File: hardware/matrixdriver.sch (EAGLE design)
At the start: 46 parts, among them IC1 75176AD, IC2 4017D, IC4 7805T, J1 DCJ0202, Q1 CSM-7X-DU, Q2 MMBT4403LT1SMD, Q3 MMBT4403LT1SMD, Q4 MMBT4403LT1SMD, Q5 MMBT4403LT1SMD, Q6 MMBT4403LT1SMD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

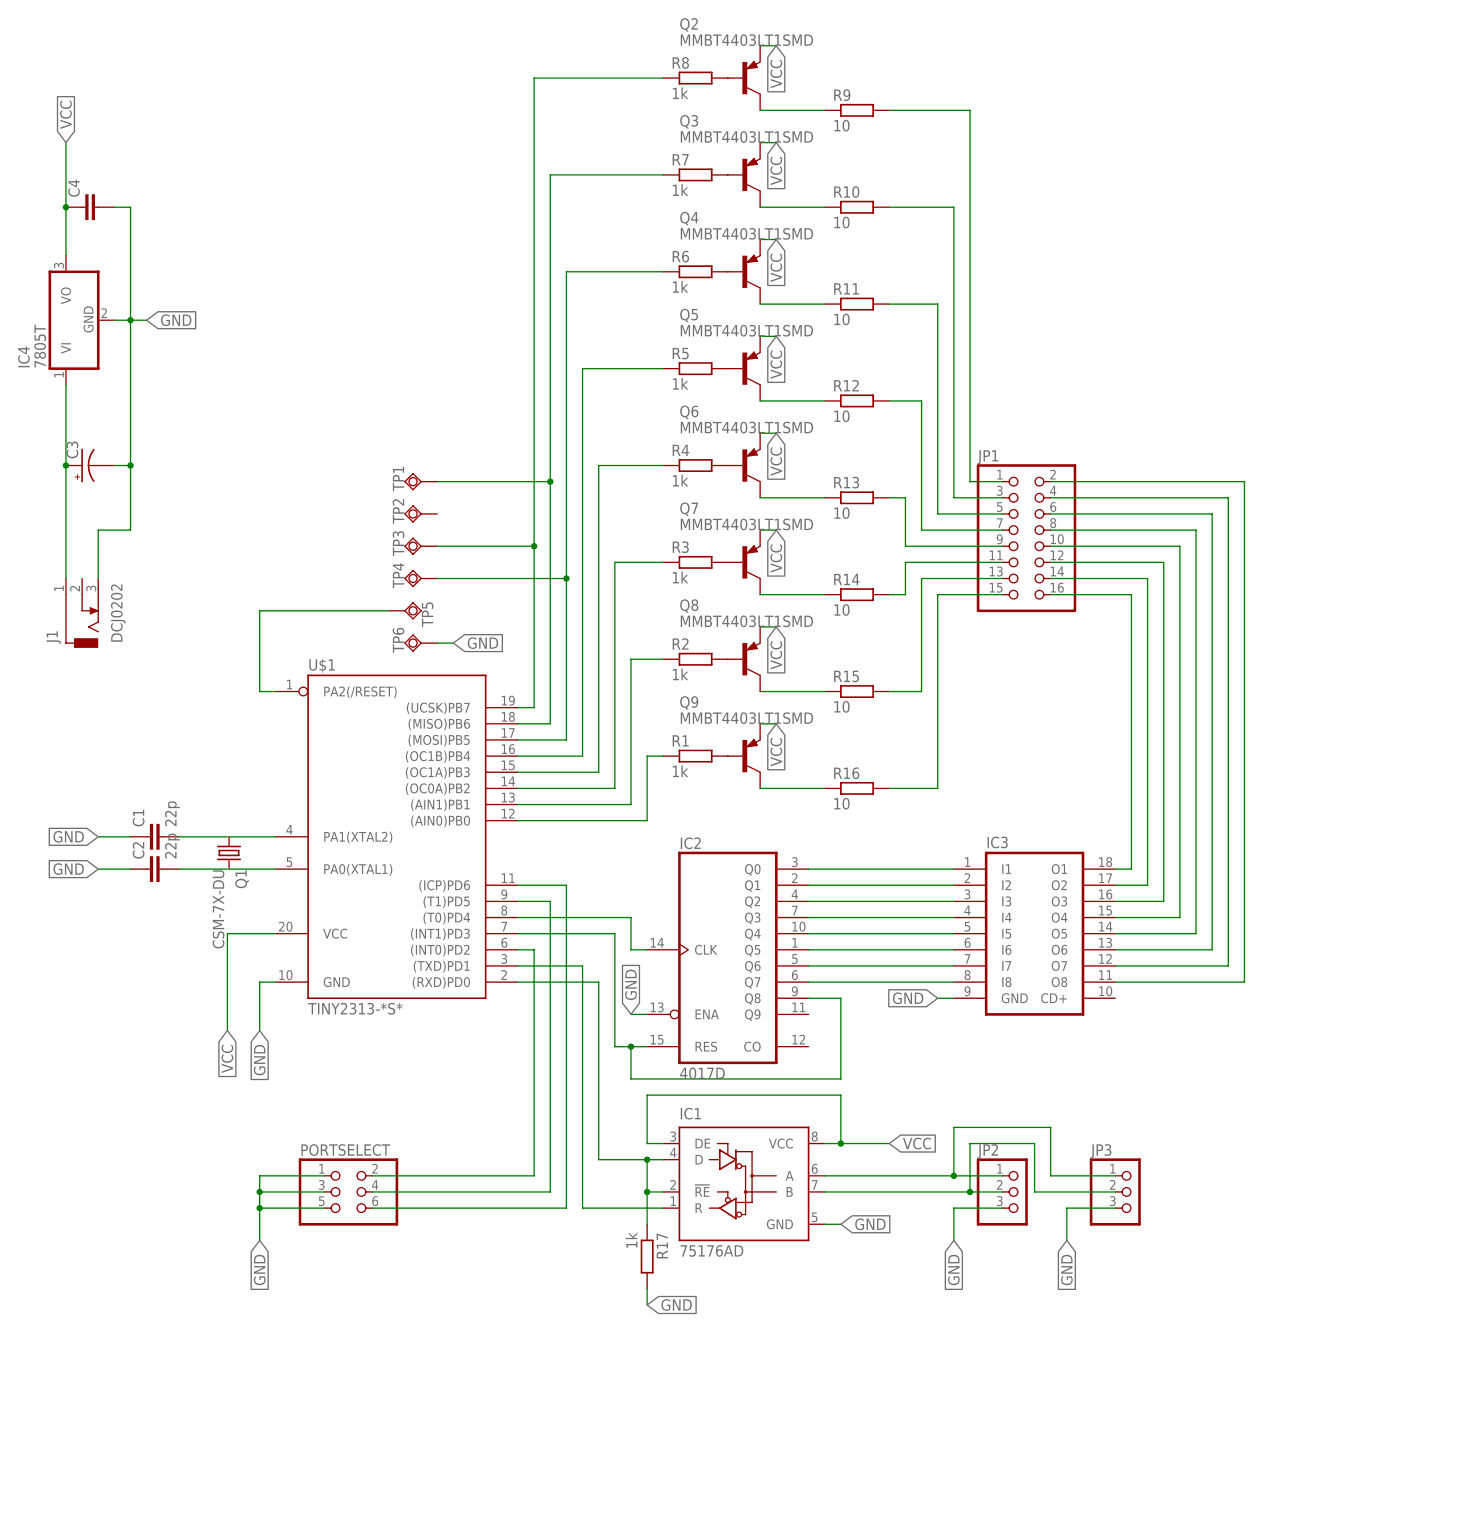
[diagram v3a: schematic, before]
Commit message: Fix Schematic ERC rrors
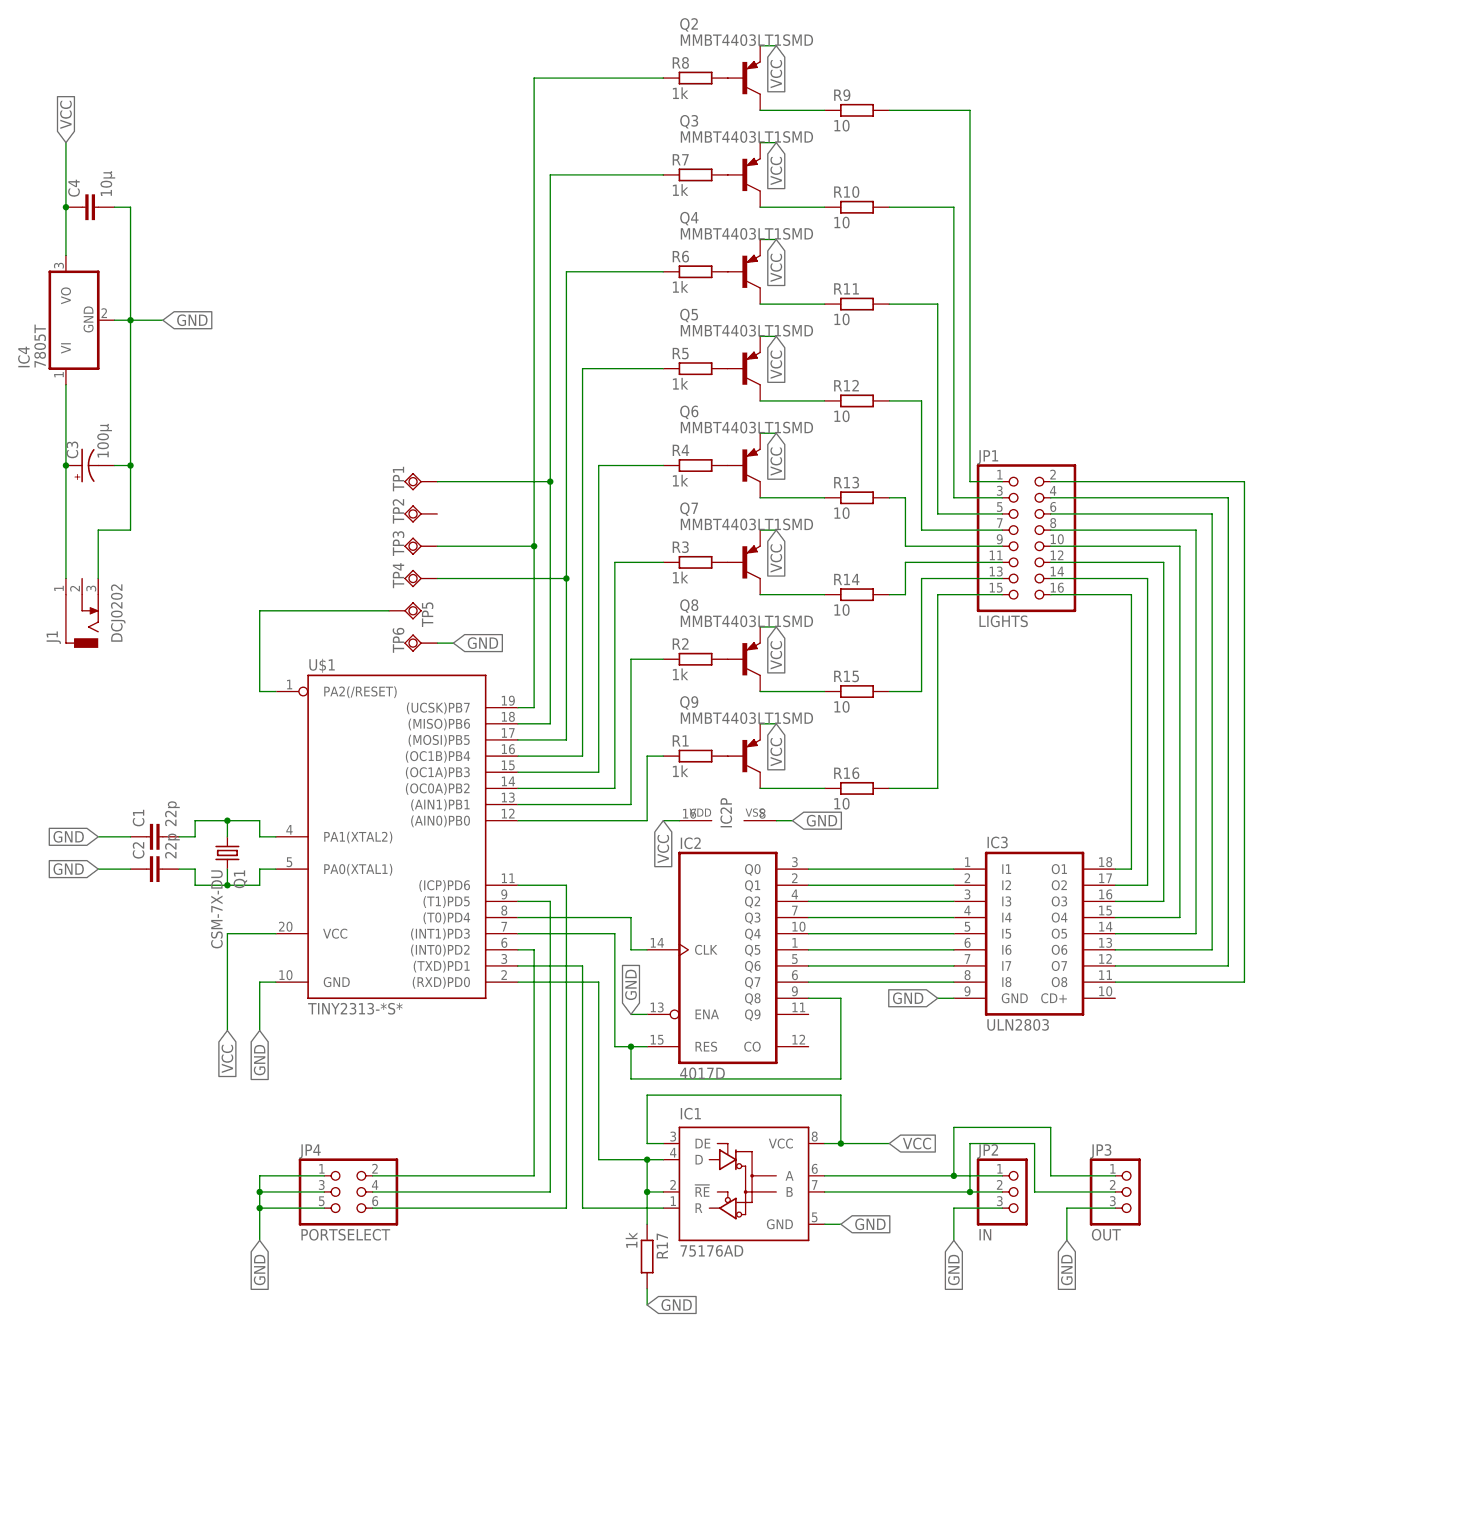
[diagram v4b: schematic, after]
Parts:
- C3: value (none) -> 100µ
- C4: value (none) -> 10µ
- IC3: value (none) -> ULN2803
- JP1: value (none) -> LIGHTS
- JP2: value (none) -> IN
- JP3: value (none) -> OUT
- JP4: value (none) -> PORTSELECT
- renumbered PORTSELECT to JP4
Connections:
- removed net N$13: C1.2
- removed net N$14: C2.2
- net GND: now also IC2P.VSS
- net N$11: now also C1.2
- net N$12: now also C2.2
- net VCC: now also IC2P.VDD
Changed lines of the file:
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@@
 <part name="C2" library="resistor" deviceset="C-EU" device="C1206" value="22p"/>
 <part name="IC2" library="40xx" deviceset="4017" device="D"/>
-<part name="IC3" library="uln-udn" deviceset="ULN2803A" device="SMD"/>
-<part name="JP1" library="pinhead-fixdrills" deviceset="PINHD-2X8" device="_2.54-90°"/>
+<part name="IC3" library="uln-udn" deviceset="ULN2803A" device="SMD" value="ULN2803"/>
+<part name="JP1" library="pinhead-fixdrills" deviceset="PINHD-2X8" device="_2.54-90°" value="LIGHTS"/>
 <part name="Q2" library="transistor-pnp" deviceset="MMBT4403*" device="SMD" technology="LT1"/>
 <part name="Q3" library="transistor-pnp" deviceset="MMBT4403*" device="SMD" technology="LT1"/>
@@
 <part name="Q8" library="transistor-pnp" deviceset="MMBT4403*" device="SMD" technology="LT1"/>
 <part name="Q9" library="transistor-pnp" deviceset="MMBT4403*" device="SMD" technology="LT1"/>
-<part name="JP2" library="pinhead" deviceset="PINHD-1X3" device=""/>
-<part name="JP3" library="pinhead" deviceset="PINHD-1X3" device=""/>
+<part name="JP2" library="pinhead" deviceset="PINHD-1X3" device="" value="IN"/>
+<part name="JP3" library="pinhead" deviceset="PINHD-1X3" device="" value="OUT"/>
 <part name="TP1" library="testpad" deviceset="TPSQ" device="TP20SQ"/>
 <part name="TP2" library="testpad" deviceset="TPSQ" device="TP20SQ"/>
@@
 <part name="TP5" library="testpad" deviceset="TPSQ" device="TP20SQ"/>
 <part name="TP6" library="testpad" deviceset="TPSQ" device="TP20SQ"/>
-<part name="PORTSELECT" library="pinhead" deviceset="PINHD-2X3" device=""/>
+<part name="JP4" library="pinhead" deviceset="PINHD-2X3" device="" value="PORTSELECT"/>
 <part name="IC4" library="linear" deviceset="78*" device="T" technology="05"/>
-<part name="C3" library="rcl" deviceset="CPOL-US" device="E5-8.5"/>
-<part name="C4" library="rcl" deviceset="C-EU" device="C1206"/>
+<part name="C3" library="rcl" deviceset="CPOL-US" device="E5-8.5" value="100µ"/>
+<part name="C4" library="rcl" deviceset="C-EU" device="C1206" value="10µ"/>
 <part name="J1" library="con-jack" deviceset="DCJ0202" device=""/>
 </parts>
@@
 <instance part="R15" gate="G$1" x="129.54" y="93.98"/>
 <instance part="R16" gate="G$1" x="129.54" y="78.74"/>
-<instance part="Q1" gate="P" x="30.734" y="68.58" rot="R270"/>
+<instance part="Q1" gate="P" x="30.48" y="68.58" rot="R270"/>
 <instance part="IC1" gate="G$1" x="111.76" y="17.78"/>
 <instance part="R17" gate="G$1" x="96.52" y="5.08" rot="R270"/>
@@
 <instance part="TP5" gate="G$1" x="58.42" y="106.68" rot="R90"/>
 <instance part="TP6" gate="G$1" x="60.96" y="101.6" rot="R270"/>
-<instance part="PORTSELECT" gate="A" x="48.26" y="15.24"/>
+<instance part="JP4" gate="A" x="48.26" y="15.24"/>
 <instance part="IC4" gate="A1" x="5.08" y="152.4" rot="R90"/>
 <instance part="C3" gate="G$1" x="7.62" y="129.54" rot="R90"/>
 <instance part="C4" gate="G$1" x="7.62" y="170.18" rot="R90"/>
 <instance part="J1" gate="G$1" x="7.62" y="104.14" rot="R90"/>
+<instance part="IC2" gate="P" x="109.22" y="73.66" rot="R90"/>
 </instances>
 <busses>
@@
 <label x="5.08" y="180.34" size="1.778" layer="95" rot="R90" xref="yes"/>
 </segment>
+<segment>
+<pinref part="IC2" gate="P" pin="VDD"/>
+<wire x1="101.6" y1="73.66" x2="99.06" y2="73.66" width="0.1524" layer="91"/>
+<label x="99.06" y="73.66" size="1.778" layer="95" rot="R270" xref="yes"/>
+</segment>
 </net>
 <net name="GND" class="0">
@@
 </segment>
 <segment>
-<pinref part="PORTSELECT" gate="A" pin="1"/>
+<pinref part="JP4" gate="A" pin="1"/>
 <wire x1="45.72" y1="17.78" x2="35.56" y2="17.78" width="0.1524" layer="91"/>
 <wire x1="35.56" y1="17.78" x2="35.56" y2="15.24" width="0.1524" layer="91"/>
-<pinref part="PORTSELECT" gate="A" pin="3"/>
+<pinref part="JP4" gate="A" pin="3"/>
 <wire x1="35.56" y1="15.24" x2="35.56" y2="12.7" width="0.1524" layer="91"/>
 <wire x1="35.56" y1="12.7" x2="35.56" y2="7.62" width="0.1524" layer="91"/>
 <wire x1="45.72" y1="15.24" x2="35.56" y2="15.24" width="0.1524" layer="91"/>
 <junction x="35.56" y="15.24"/>
-<pinref part="PORTSELECT" gate="A" pin="5"/>
+<pinref part="JP4" gate="A" pin="5"/>
 <wire x1="45.72" y1="12.7" x2="35.56" y2="12.7" width="0.1524" layer="91"/>
 <junction x="35.56" y="12.7"/>
@@
 <pinref part="IC4" gate="A1" pin="GND"/>
 <wire x1="12.7" y1="152.4" x2="15.24" y2="152.4" width="0.1524" layer="91"/>
-<label x="17.78" y="152.4" size="1.778" layer="95" xref="yes"/>
+<label x="20.32" y="152.4" size="1.778" layer="95" xref="yes"/>
 <pinref part="J1" gate="G$1" pin="3"/>
-<wire x1="15.24" y1="152.4" x2="17.78" y2="152.4" width="0.1524" layer="91"/>
+<wire x1="15.24" y1="152.4" x2="20.32" y2="152.4" width="0.1524" layer="91"/>
 <wire x1="10.16" y1="111.76" x2="10.16" y2="119.38" width="0.1524" layer="91"/>
 <wire x1="10.16" y1="119.38" x2="15.24" y2="119.38" width="0.1524" layer="91"/>
@@
 <junction x="15.24" y="129.54"/>
 </segment>
-</net>
-<net name="N$11" class="0">
-<segment>
-<pinref part="U$1" gate="G$1" pin="PA1(XTAL2)"/>
-<wire x1="38.1" y1="71.12" x2="30.734" y2="71.12" width="0.1524" layer="91"/>
-<pinref part="Q1" gate="P" pin="1"/>
-</segment>
-</net>
-<net name="N$12" class="0">
-<segment>
-<pinref part="U$1" gate="G$1" pin="PA0(XTAL1)"/>
-<wire x1="38.1" y1="66.04" x2="30.734" y2="66.04" width="0.1524" layer="91"/>
-<pinref part="Q1" gate="P" pin="2"/>
-</segment>
-</net>
-<net name="N$13" class="0">
-<segment>
-<pinref part="C1" gate="G$1" pin="2"/>
-<wire x1="30.48" y1="71.12" x2="22.86" y2="71.12" width="0.1524" layer="91"/>
-</segment>
-</net>
-<net name="N$14" class="0">
-<segment>
-<pinref part="C2" gate="G$1" pin="2"/>
-<wire x1="30.48" y1="66.04" x2="22.86" y2="66.04" width="0.1524" layer="91"/>
+<segment>
+<pinref part="IC2" gate="P" pin="VSS"/>
+<wire x1="116.84" y1="73.66" x2="119.38" y2="73.66" width="0.1524" layer="91"/>
+<label x="119.38" y="73.66" size="1.778" layer="95" xref="yes"/>
 </segment>
 </net>
@@
 <net name="N$60" class="0">
 <segment>
-<pinref part="PORTSELECT" gate="A" pin="2"/>
+<pinref part="JP4" gate="A" pin="2"/>
 <wire x1="53.34" y1="17.78" x2="78.74" y2="17.78" width="0.1524" layer="91"/>
 <wire x1="78.74" y1="17.78" x2="78.74" y2="53.34" width="0.1524" layer="91"/>
@@
 <net name="N$61" class="0">
 <segment>
-<pinref part="PORTSELECT" gate="A" pin="4"/>
+<pinref part="JP4" gate="A" pin="4"/>
 <wire x1="53.34" y1="15.24" x2="81.28" y2="15.24" width="0.1524" layer="91"/>
 <wire x1="81.28" y1="15.24" x2="81.28" y2="60.96" width="0.1524" layer="91"/>
@@
 <net name="N$62" class="0">
 <segment>
-<pinref part="PORTSELECT" gate="A" pin="6"/>
+<pinref part="JP4" gate="A" pin="6"/>
 <wire x1="53.34" y1="12.7" x2="83.82" y2="12.7" width="0.1524" layer="91"/>
 <wire x1="83.82" y1="12.7" x2="83.82" y2="63.5" width="0.1524" layer="91"/>
@@
 </segment>
 </net>
+<net name="N$11" class="0">
+<segment>
+<pinref part="C1" gate="G$1" pin="2"/>
+<wire x1="22.86" y1="71.12" x2="25.4" y2="71.12" width="0.1524" layer="91"/>
+<wire x1="25.4" y1="71.12" x2="25.4" y2="73.66" width="0.1524" layer="91"/>
+<wire x1="25.4" y1="73.66" x2="30.48" y2="73.66" width="0.1524" layer="91"/>
+<wire x1="30.48" y1="73.66" x2="35.56" y2="73.66" width="0.1524" layer="91"/>
+<wire x1="35.56" y1="73.66" x2="35.56" y2="71.12" width="0.1524" layer="91"/>
+<pinref part="U$1" gate="G$1" pin="PA1(XTAL2)"/>
+<wire x1="35.56" y1="71.12" x2="38.1" y2="71.12" width="0.1524" layer="91"/>
+<wire x1="30.48" y1="71.12" x2="30.48" y2="73.66" width="0.1524" layer="91"/>
+<junction x="30.48" y="73.66"/>
+<pinref part="Q1" gate="P" pin="1"/>
+</segment>
+</net>
+<net name="N$12" class="0">
+<segment>
+<pinref part="U$1" gate="G$1" pin="PA0(XTAL1)"/>
+<wire x1="38.1" y1="66.04" x2="35.56" y2="66.04" width="0.1524" layer="91"/>
+<wire x1="35.56" y1="66.04" x2="35.56" y2="63.5" width="0.1524" layer="91"/>
+<wire x1="35.56" y1="63.5" x2="30.48" y2="63.5" width="0.1524" layer="91"/>
+<wire x1="30.48" y1="63.5" x2="25.4" y2="63.5" width="0.1524" layer="91"/>
+<wire x1="25.4" y1="63.5" x2="25.4" y2="66.04" width="0.1524" layer="91"/>
+<pinref part="C2" gate="G$1" pin="2"/>
+<wire x1="25.4" y1="66.04" x2="22.86" y2="66.04" width="0.1524" layer="91"/>
+<pinref part="Q1" gate="P" pin="2"/>
+<wire x1="30.48" y1="63.5" x2="30.48" y2="66.04" width="0.1524" layer="91"/>
+<junction x="30.48" y="63.5"/>
+</segment>
+</net>
 </nets>
 </sheet>
 </sheets>
+<errors>
+</errors>
 </schematic>
 </drawing>

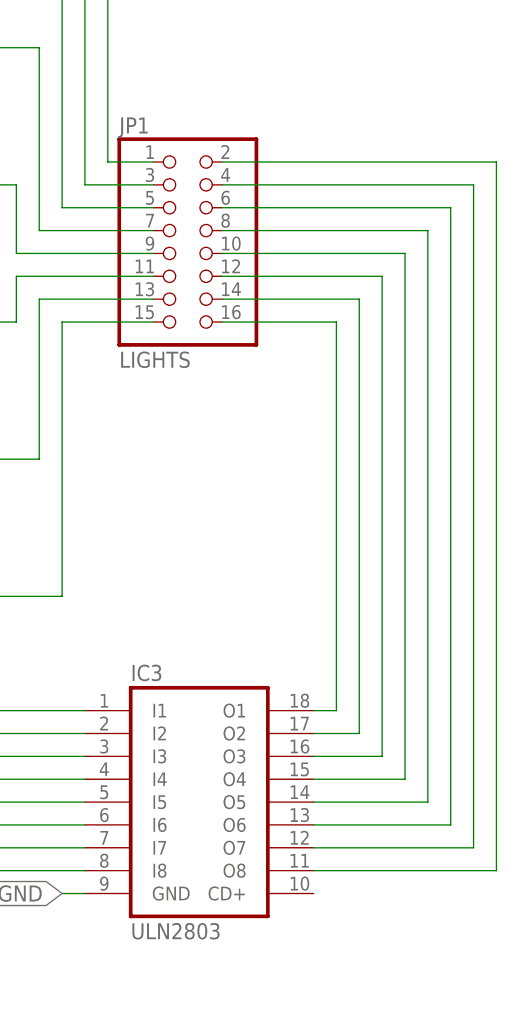
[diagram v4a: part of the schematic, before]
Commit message: Add first board layout
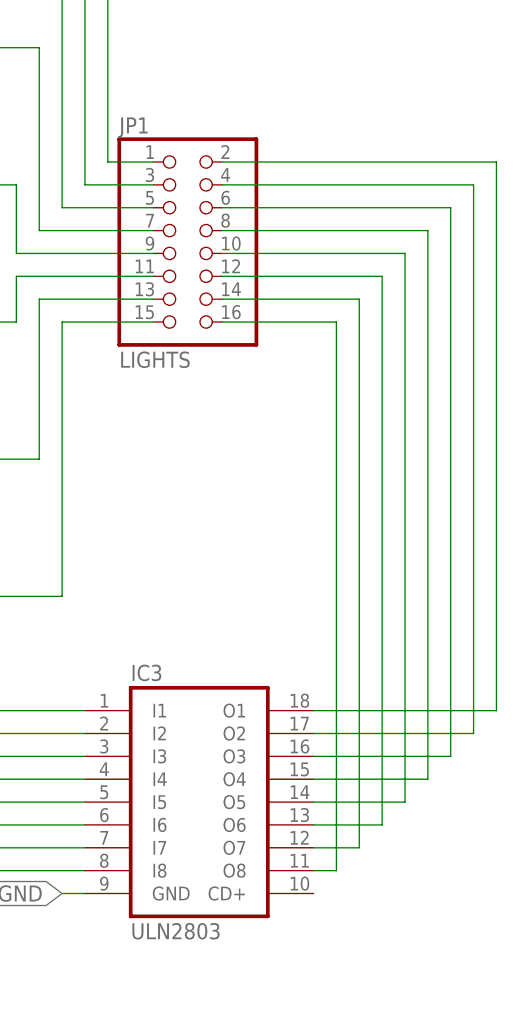
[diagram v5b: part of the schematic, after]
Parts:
- TP1: value TPSQTP20SQ -> TPSQTP20R; device testpad:TPSQTP20SQ -> testpad:TPSQTP20R
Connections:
- removed net N$29: IC3.O5, JP1.8
- removed net N$30: IC3.O6, JP1.6
- removed net N$31: IC3.O7, JP1.4
- removed net N$32: IC3.O8, JP1.2
- new net N$14: IC3.O1, JP1.2
- new net N$63: IC3.O2, JP1.4
- new net N$64: IC3.O3, JP1.6
- new net N$66: IC3.O4, JP1.8
- net N$25: now also IC3.O8; no longer IC3.O1
- net N$26: now also IC3.O7; no longer IC3.O2
- net N$27: now also IC3.O6; no longer IC3.O3
- net N$28: now also IC3.O5; no longer IC3.O4
